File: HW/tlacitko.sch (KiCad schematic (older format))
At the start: 2 parts

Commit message: add some codes for JLCPCB, change package and schematic of CP2102
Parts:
- C?: LCSC (none) -> C15195
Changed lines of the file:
@@
 F 2 "Capacitor_SMD:C_0402_1005Metric" H 3788 2850 50  0001 C CNN
 F 3 "~" H 3750 3000 50  0001 C CNN
+F 4 "C15195" H 3750 3000 50  0001 C CNN "LCSC"
 	1    3750 3000
 	0    1    1    0

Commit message: add footprint of inductor, add codes for JLCPCB, repair mistakes
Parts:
- SW?: LCSC (none) -> ručně
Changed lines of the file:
@@
 F 2 "Button_Switch_THT:SW_Tactile_Straight_KSL0Axx1LFTR" H 3750 3000 50  0001 C CNN
 F 3 "~" H 3750 3000 50  0001 C CNN
+F 4 "ručně" H 3750 2800 50  0001 C CNN "LCSC"
 	1    3750 2800
 	1    0    0    -1

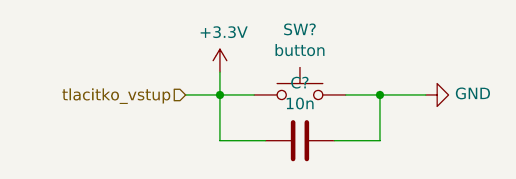
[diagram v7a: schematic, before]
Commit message: numbering components, place components on board
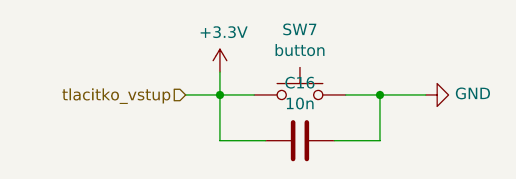
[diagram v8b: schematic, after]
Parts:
- gave numbers to parts that had none: 2
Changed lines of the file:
@@
 $Descr A4 11693 8268
 encoding utf-8
-Sheet 7 44
+Sheet 9 44
 Title ""
 Date ""
@@
 AR Path="/5F76AB3F" Ref="SW?"  Part="1"
 AR Path="/5FB92F8B/5F76AB3F" Ref="SW?"  Part="1"
-AR Path="/5FB92F8B/5F768D65/5F76AB3F" Ref="SW?"  Part="1"
-AR Path="/5FB92F8B/5F76BB44/5F76AB3F" Ref="SW?"  Part="1"
-AR Path="/5FB92F8B/5F76DF12/5F76AB3F" Ref="SW?"  Part="1"
-AR Path="/5FB92F8B/5F76E918/5F76AB3F" Ref="SW?"  Part="1"
-AR Path="/5FB92F8B/5F76EE0D/5F76AB3F" Ref="SW?"  Part="1"
-AR Path="/5FB92F8B/5F76F2AA/5F76AB3F" Ref="SW?"  Part="1"
-AR Path="/5FB92F8B/5F76F385/5F76AB3F" Ref="SW?"  Part="1"
-F 0 "SW?" H 3750 3085 50  0000 C CNN
+AR Path="/5FB92F8B/5F768D65/5F76AB3F" Ref="SW2"  Part="1"
+AR Path="/5FB92F8B/5F76BB44/5F76AB3F" Ref="SW3"  Part="1"
+AR Path="/5FB92F8B/5F76DF12/5F76AB3F" Ref="SW4"  Part="1"
+AR Path="/5FB92F8B/5F76E918/5F76AB3F" Ref="SW5"  Part="1"
+AR Path="/5FB92F8B/5F76EE0D/5F76AB3F" Ref="SW6"  Part="1"
+AR Path="/5FB92F8B/5F76F2AA/5F76AB3F" Ref="SW7"  Part="1"
+AR Path="/5FB92F8B/5F76F385/5F76AB3F" Ref="SW8"  Part="1"
+F 0 "SW7" H 3750 3085 50  0000 C CNN
 F 1 "button" H 3750 2994 50  0000 C CNN
 F 2 "Button_Switch_THT:SW_Tactile_Straight_KSL0Axx1LFTR" H 3750 3000 50  0001 C CNN
@@
 AR Path="/5F76AB45" Ref="C?"  Part="1"
 AR Path="/5FB92F8B/5F76AB45" Ref="C?"  Part="1"
-AR Path="/5FB92F8B/5F768D65/5F76AB45" Ref="C?"  Part="1"
-AR Path="/5FB92F8B/5F76BB44/5F76AB45" Ref="C?"  Part="1"
-AR Path="/5FB92F8B/5F76DF12/5F76AB45" Ref="C?"  Part="1"
-AR Path="/5FB92F8B/5F76E918/5F76AB45" Ref="C?"  Part="1"
-AR Path="/5FB92F8B/5F76EE0D/5F76AB45" Ref="C?"  Part="1"
-AR Path="/5FB92F8B/5F76F2AA/5F76AB45" Ref="C?"  Part="1"
-AR Path="/5FB92F8B/5F76F385/5F76AB45" Ref="C?"  Part="1"
-F 0 "C?" V 3498 3000 50  0000 C CNN
+AR Path="/5FB92F8B/5F768D65/5F76AB45" Ref="C11"  Part="1"
+AR Path="/5FB92F8B/5F76BB44/5F76AB45" Ref="C12"  Part="1"
+AR Path="/5FB92F8B/5F76DF12/5F76AB45" Ref="C13"  Part="1"
+AR Path="/5FB92F8B/5F76E918/5F76AB45" Ref="C14"  Part="1"
+AR Path="/5FB92F8B/5F76EE0D/5F76AB45" Ref="C15"  Part="1"
+AR Path="/5FB92F8B/5F76F2AA/5F76AB45" Ref="C16"  Part="1"
+AR Path="/5FB92F8B/5F76F385/5F76AB45" Ref="C17"  Part="1"
+F 0 "C16" V 3498 3000 50  0000 C CNN
 F 1 "10n" V 3589 3000 50  0000 C CNN
 F 2 "Capacitor_SMD:C_0402_1005Metric" H 3788 2850 50  0001 C CNN
@@
 AR Path="/5F76AB53" Ref="#PWR?"  Part="1"
 AR Path="/5FB92F8B/5F76AB53" Ref="#PWR?"  Part="1"
-AR Path="/5FB92F8B/5F768D65/5F76AB53" Ref="#PWR?"  Part="1"
-AR Path="/5FB92F8B/5F76BB44/5F76AB53" Ref="#PWR?"  Part="1"
-AR Path="/5FB92F8B/5F76DF12/5F76AB53" Ref="#PWR?"  Part="1"
-AR Path="/5FB92F8B/5F76E918/5F76AB53" Ref="#PWR?"  Part="1"
-AR Path="/5FB92F8B/5F76EE0D/5F76AB53" Ref="#PWR?"  Part="1"
-AR Path="/5FB92F8B/5F76F2AA/5F76AB53" Ref="#PWR?"  Part="1"
-AR Path="/5FB92F8B/5F76F385/5F76AB53" Ref="#PWR?"  Part="1"
-F 0 "#PWR?" H 4300 2550 50  0001 C CNN
+AR Path="/5FB92F8B/5F768D65/5F76AB53" Ref="#PWR0115"  Part="1"
+AR Path="/5FB92F8B/5F76BB44/5F76AB53" Ref="#PWR0117"  Part="1"
+AR Path="/5FB92F8B/5F76DF12/5F76AB53" Ref="#PWR0119"  Part="1"
+AR Path="/5FB92F8B/5F76E918/5F76AB53" Ref="#PWR0121"  Part="1"
+AR Path="/5FB92F8B/5F76EE0D/5F76AB53" Ref="#PWR0123"  Part="1"
+AR Path="/5FB92F8B/5F76F2AA/5F76AB53" Ref="#PWR0125"  Part="1"
+AR Path="/5FB92F8B/5F76F385/5F76AB53" Ref="#PWR0127"  Part="1"
+F 0 "#PWR0125" H 4300 2550 50  0001 C CNN
 F 1 "GND" V 4305 2672 50  0000 R CNN
 F 2 "" H 4300 2800 50  0001 C CNN
@@
 AR Path="/5F76AB5B" Ref="#PWR?"  Part="1"
 AR Path="/5FB92F8B/5F76AB5B" Ref="#PWR?"  Part="1"
-AR Path="/5FB92F8B/5F768D65/5F76AB5B" Ref="#PWR?"  Part="1"
-AR Path="/5FB92F8B/5F76BB44/5F76AB5B" Ref="#PWR?"  Part="1"
-AR Path="/5FB92F8B/5F76DF12/5F76AB5B" Ref="#PWR?"  Part="1"
-AR Path="/5FB92F8B/5F76E918/5F76AB5B" Ref="#PWR?"  Part="1"
-AR Path="/5FB92F8B/5F76EE0D/5F76AB5B" Ref="#PWR?"  Part="1"
-AR Path="/5FB92F8B/5F76F2AA/5F76AB5B" Ref="#PWR?"  Part="1"
-AR Path="/5FB92F8B/5F76F385/5F76AB5B" Ref="#PWR?"  Part="1"
-F 0 "#PWR?" H 3400 2550 50  0001 C CNN
+AR Path="/5FB92F8B/5F768D65/5F76AB5B" Ref="#PWR0116"  Part="1"
+AR Path="/5FB92F8B/5F76BB44/5F76AB5B" Ref="#PWR0118"  Part="1"
+AR Path="/5FB92F8B/5F76DF12/5F76AB5B" Ref="#PWR0120"  Part="1"
+AR Path="/5FB92F8B/5F76E918/5F76AB5B" Ref="#PWR0122"  Part="1"
+AR Path="/5FB92F8B/5F76EE0D/5F76AB5B" Ref="#PWR0124"  Part="1"
+AR Path="/5FB92F8B/5F76F2AA/5F76AB5B" Ref="#PWR0126"  Part="1"
+AR Path="/5FB92F8B/5F76F385/5F76AB5B" Ref="#PWR0128"  Part="1"
+F 0 "#PWR0126" H 3400 2550 50  0001 C CNN
 F 1 "+3.3V" H 3415 2873 50  0000 C CNN
 F 2 "" H 3400 2700 50  0001 C CNN
